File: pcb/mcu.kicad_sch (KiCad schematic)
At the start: 11 parts, among them U3 IC_MCU_STM32F100C4T6B_48LQFP, X1 XTAL_32K768_7pF_ECS-.327-7-34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

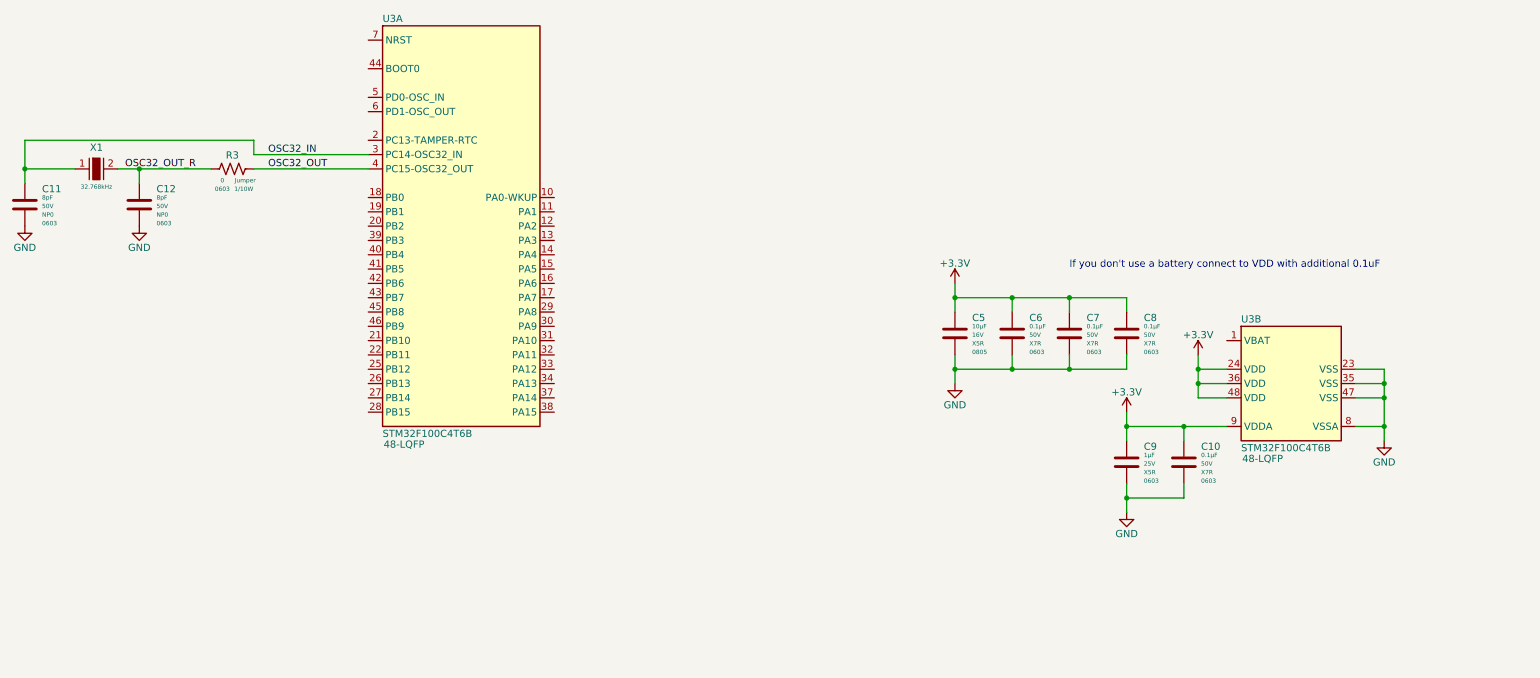
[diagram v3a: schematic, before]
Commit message: Added 8MHz Oscillator and mapped most of the MCU pins"
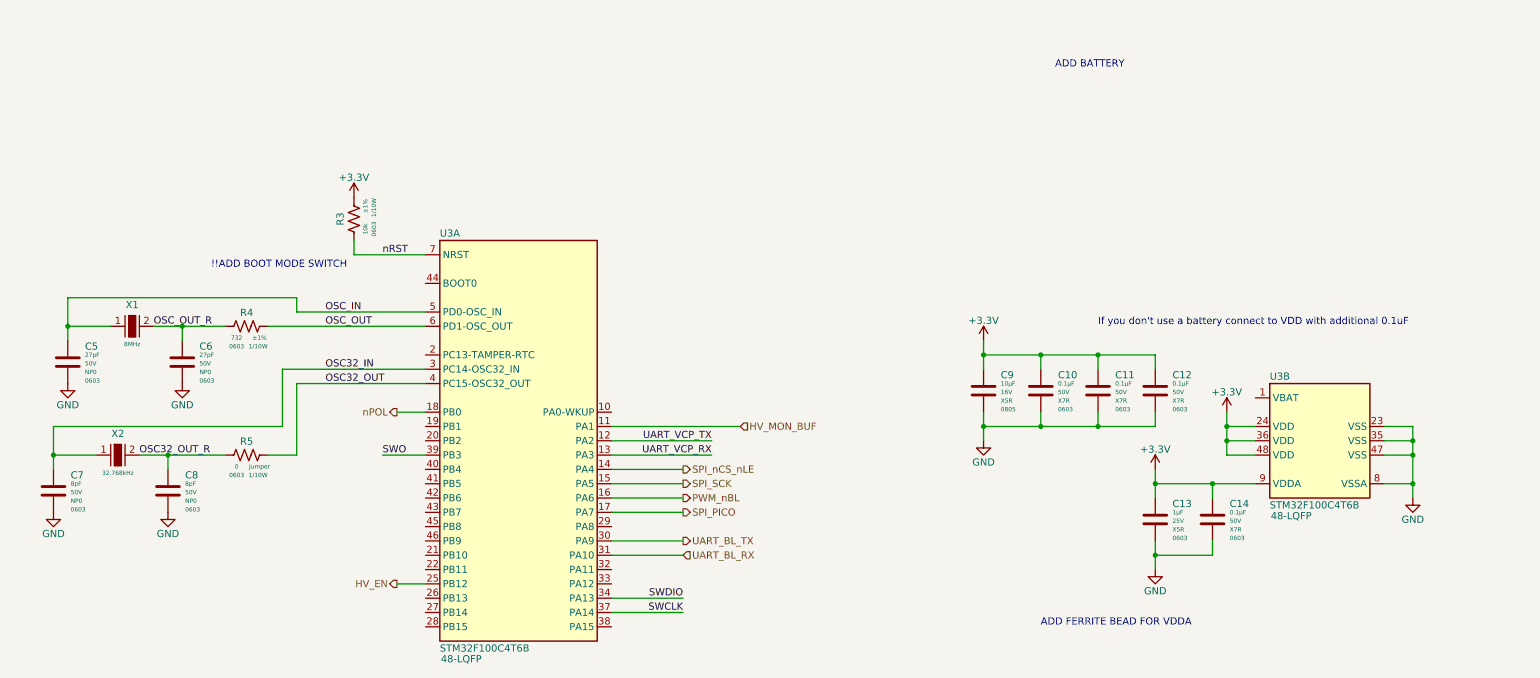
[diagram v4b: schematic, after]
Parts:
- removed X1: XTAL_32K768_7pF_ECS-.327-7-34B-C-TR, arjun_footprints:SMD-2_3.2x1.5mm, symbol arjun_symbols:XTAL_32K768_7pF_ECS-.327-7-34B-C-TR
- added C5, C6: CAP_CER_27p_50V_NP0_0603, Capacitor_SMD:C_0603_1608Metric, symbol arjun_symbols:CAP_CER_27p_50V_NP0_0603
- added R3: RES_10K_1P_1/10W_0603, Resistor_SMD:R_0603_1608Metric, symbol arjun_symbols:RES_10K_1P_1/10W_0603
- added R4: RES_732R_1P_1/10W_0603, Resistor_SMD:R_0603_1608Metric, symbol arjun_symbols:RES_732R_1P_1/10W_0603
- added X1: XTAL_8M_20PPM_18pF_ECS-80-18-30-JGN-TR, arjun_footprints:SMD-2_5x3.2mm_ECS, symbol arjun_symbols:XTAL_8M_20PPM_18pF_ECS-80-18-30-JGN-TR
- added X2: XTAL_32K768_10PPM_7pF_ECS-.327-7-34B-C-TR, arjun_footprints:SMD-2_3.2x1.5mm_ECS, symbol arjun_symbols:XTAL_32K768_10PPM_7pF_ECS-.327-7-34B-C-TR
- renumbered C6 to C10, C7 to C11, C8 to C12, C9 to C13, C10 to C14, C11 to C7, C12 to C8, C5 to C9, R3 to R5
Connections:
- net +3.3V: now also R3.1
- net GND: now also C5.2, C6.2
- net OSC32_IN: now also X2.1
- net OSC32_OUT_R: now also X2.2
- net HV_MON_BUF: now reaches U3.11 (PA1)
- net UART_VCP_TX: now reaches U3.12 (PA2)
- net UART_VCP_RX: now reaches U3.13 (PA3)
- net SPI_nCS_nLE: now reaches U3.14 (PA4)
- net SPI_SCK: now reaches U3.15 (PA5)
- net PWM_nBL: now reaches U3.16 (PA6)
- net SPI_PICO: now reaches U3.17 (PA7)
- net nPOL: now reaches U3.18 (PB0)
- net HV_EN: now reaches U3.25 (PB12)
- net UART_BL_TX: now reaches U3.30 (PA9)
- net UART_BL_RX: now reaches U3.31 (PA10)
- net SWDIO: now reaches U3.34 (PA13)
- net SWCLK: now reaches U3.37 (PA14)
- net SWO: now reaches U3.39 (PB3)
- net OSC_IN: now reaches U3.5 (PD0-OSC_IN)
- net OSC_IN: now also C5.1, X1.1
- net OSC_OUT: now reaches U3.6 (PD1-OSC_OUT)
- net OSC_OUT: now also R4.1
- net nRST: now reaches U3.7 (NRST)
- net nRST: now also R3.2
- new net OSC_OUT_R: C6.1, R4.2, X1.2
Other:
- note added: "!!ADD BOOT MODE SWITCH"
- note added: "ADD BATTERY"
- note added: "ADD FERRITE BEAD FOR VDDA"
- moved on the sheet: C10, C11, C12, C13, C14, C7, C8, C9, R5, U3A, U3B
